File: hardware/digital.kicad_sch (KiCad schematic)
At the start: 0 parts

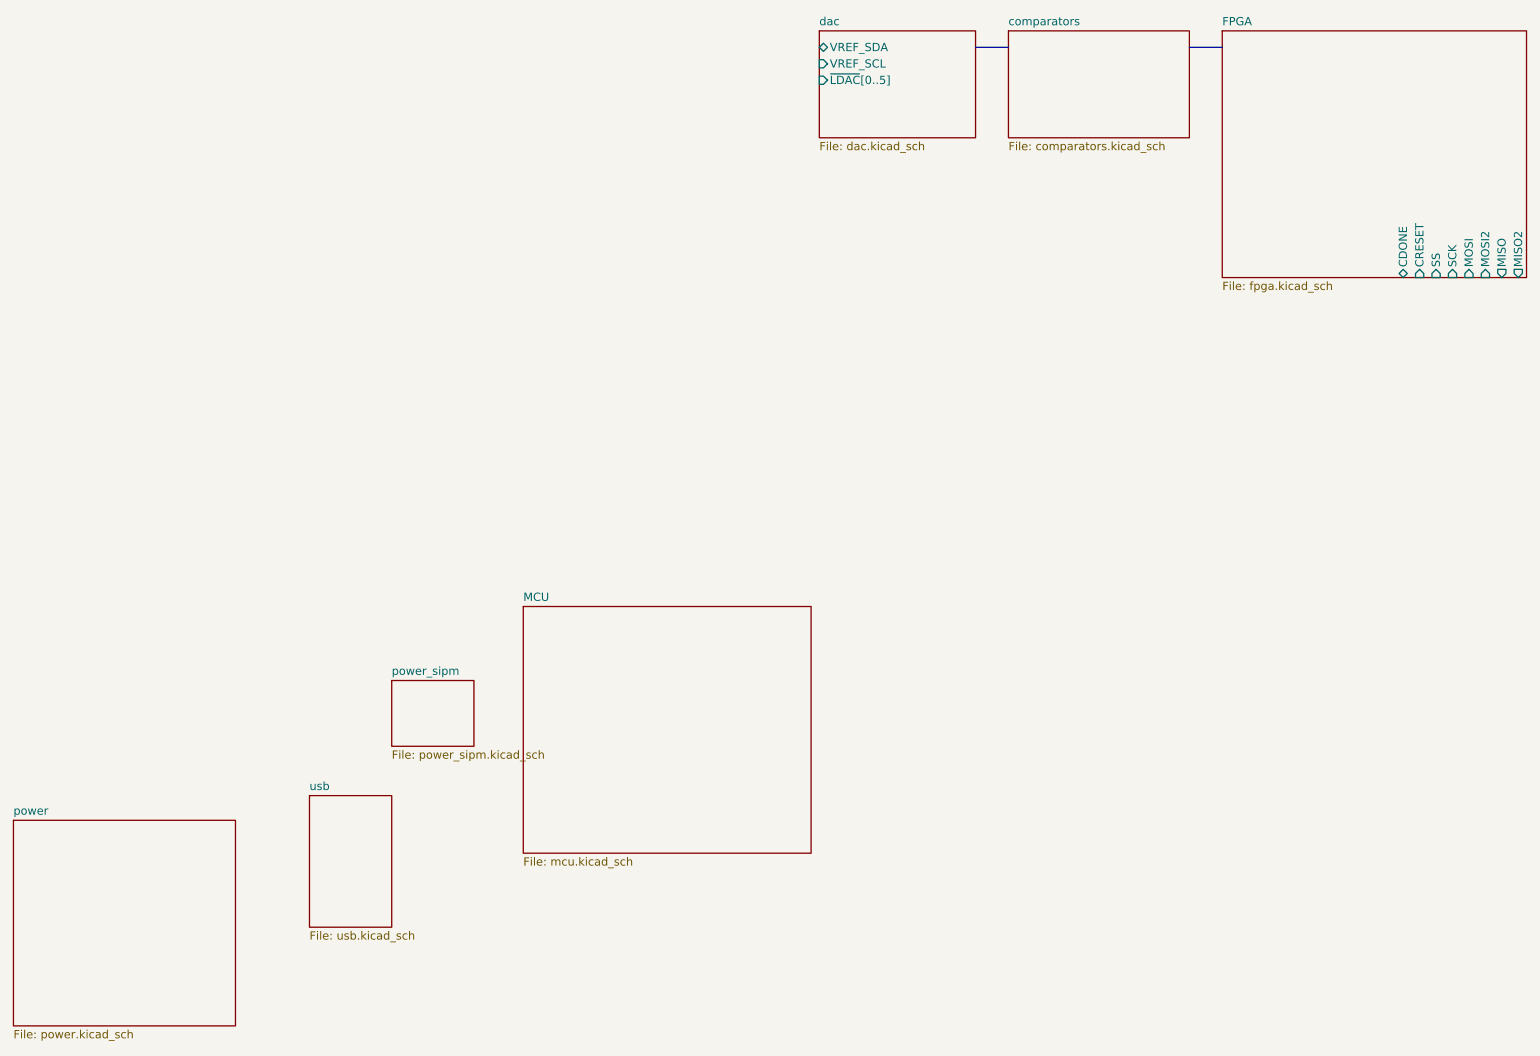
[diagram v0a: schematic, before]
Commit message: complete schematic wiring
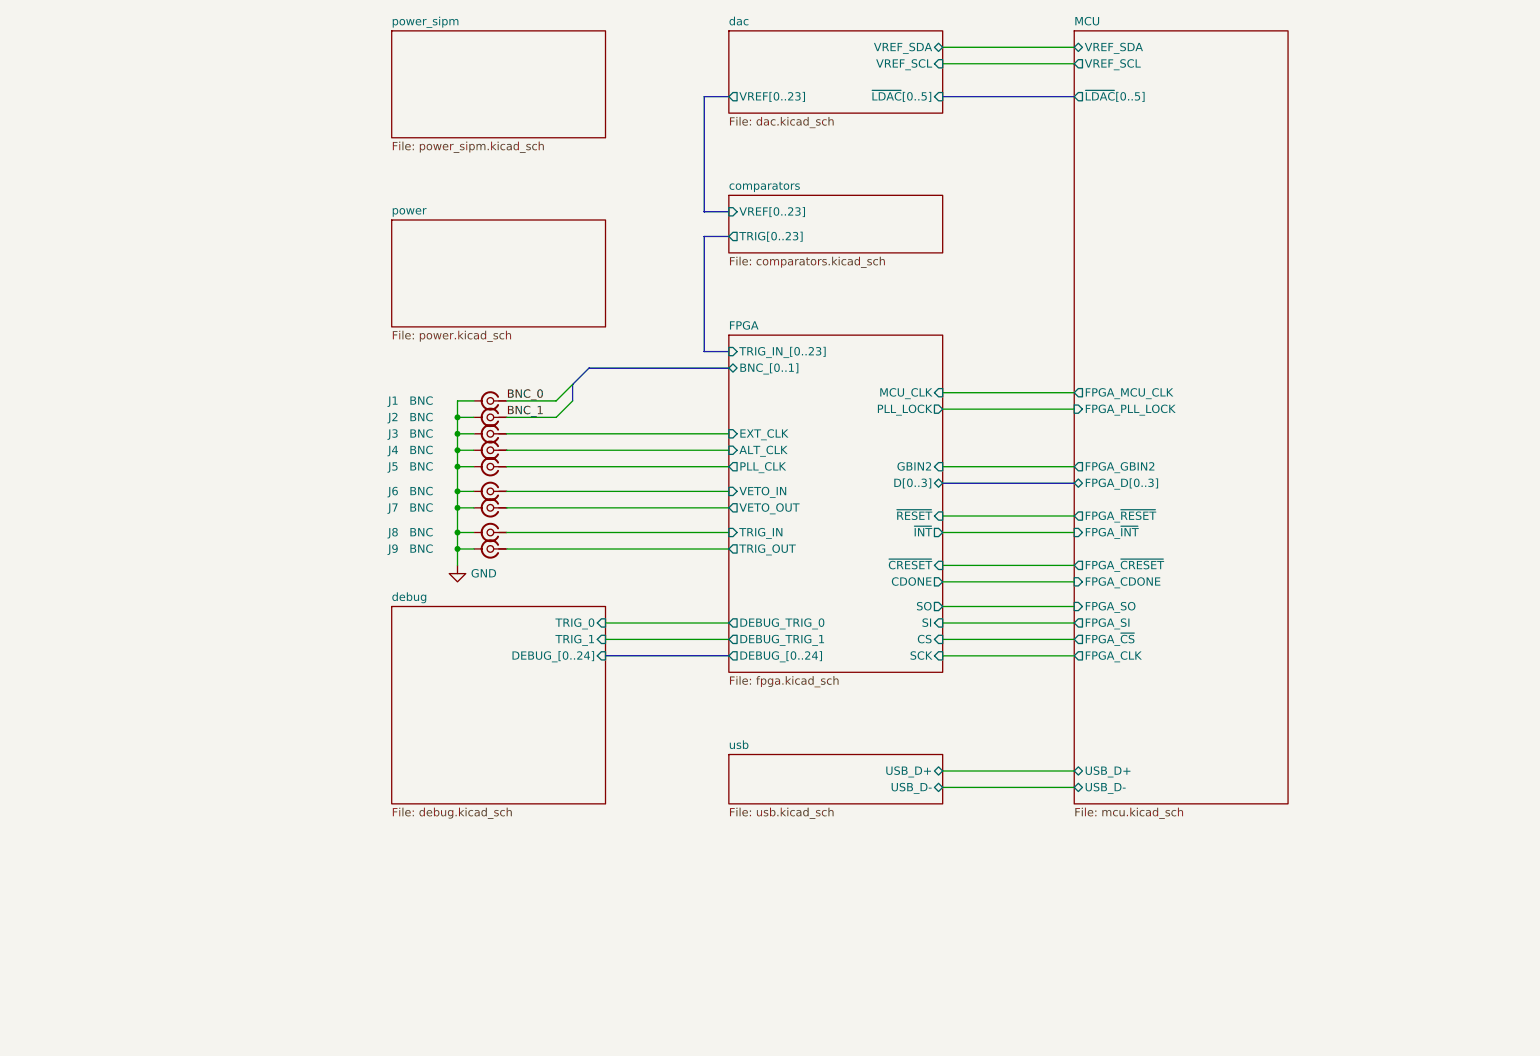
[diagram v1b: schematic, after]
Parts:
- added J1, J2, J3, J4, J5, J6, J7, J8, J9: BNC, symbol Connector:Conn_Coaxial_Small
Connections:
- new net BNC_0: J1.1 (In)
- new net BNC_1: J2.1 (In)
- new net FPGA/ALT_CLK: J4.1 (In)
- new net FPGA/EXT_CLK: J3.1 (In)
- new net FPGA/PLL_CLK: J5.1 (In)
- new net FPGA/TRIG_IN: J8.1 (In)
- new net FPGA/TRIG_OUT: J9.1 (In)
- new net FPGA/VETO_IN: J6.1 (In)
- new net FPGA/VETO_OUT: J7.1 (In)
- new net GND: J1.2 (Ext), J2.2 (Ext), J3.2 (Ext), J4.2 (Ext), J5.2 (Ext), J6.2 (Ext), J7.2 (Ext), J8.2 (Ext), J9.2 (Ext)
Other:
- added sheet debug (debug.kicad_sch)
- sheet FPGA ports: added ALT_CLK, BNC_[0..1], CS, DEBUG_TRIG_0, DEBUG_TRIG_1, DEBUG_[0..24], D[0..3], EXT_CLK, GBIN2, MCU_CLK, PLL_CLK, PLL_LOCK, SI, SO, TRIG_IN, TRIG_IN_[0..23], TRIG_OUT, VETO_IN, VETO_OUT, ~{CRESET}, ~{INT}, ~{RESET}; removed CRESET, MISO, MISO2, MOSI, MOSI2, SS
- sheet MCU ports: added FPGA_CDONE, FPGA_CLK, FPGA_D[0..3], FPGA_GBIN2, FPGA_MCU_CLK, FPGA_PLL_LOCK, FPGA_SI, FPGA_SO, FPGA_~{CRESET}, FPGA_~{CS}, FPGA_~{INT}, FPGA_~{RESET}, USB_D+, USB_D-, VREF_SCL, VREF_SDA, ~{LDAC}[0..5]; removed none
- sheet comparators ports: added TRIG[0..23], VREF[0..23]; removed none
- sheet dac ports: added VREF[0..23]; removed none
- sheet usb ports: added USB_D+, USB_D-; removed none

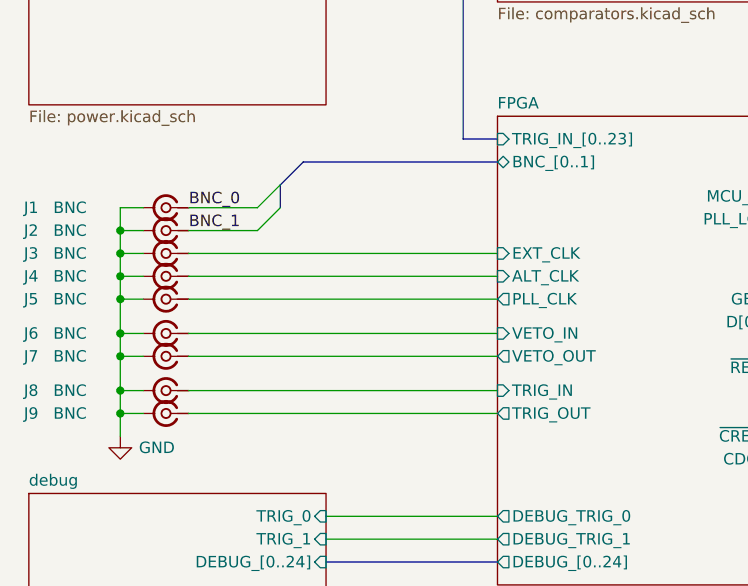
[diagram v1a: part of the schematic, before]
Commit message: update power system + add LCSC part numbers
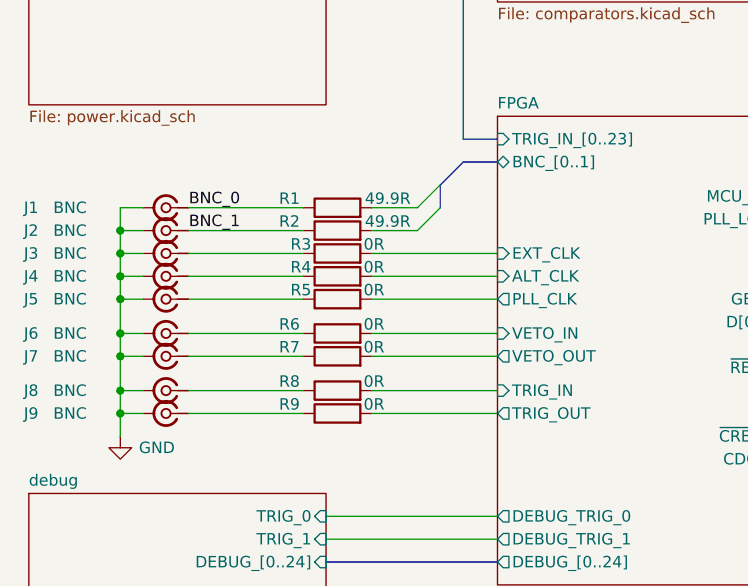
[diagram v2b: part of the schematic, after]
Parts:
- added R1, R2: 49.9R, Resistor_SMD:R_0402_1005Metric, symbol Device:R
- added R3, R4, R5, R6, R7, R8, R9: 0R, Resistor_SMD:R_0402_1005Metric, symbol Device:R
- J1, J2, J3, J4, J5, J6, J7, J8, J9: footprint (none) -> Connector_Coaxial:BNC_TEConnectivity_1478204_Vertical
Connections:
- net BNC_0: now also R1.1
- net BNC_1: now also R2.1
- net FPGA/ALT_CLK: now also R4.2; no longer J4.1 (In)
- net FPGA/EXT_CLK: now also R3.2; no longer J3.1 (In)
- net FPGA/PLL_CLK: now also R5.2; no longer J5.1 (In)
- net FPGA/TRIG_IN: now also R8.2; no longer J8.1 (In)
- net FPGA/TRIG_OUT: now also R9.2; no longer J9.1 (In)
- net FPGA/VETO_IN: now also R6.2; no longer J6.1 (In)
- net FPGA/VETO_OUT: now also R7.2; no longer J7.1 (In)
- new net: J5.1 (In), R5.1
- new net: J3.1 (In), R3.1
- new net: J7.1 (In), R7.1
- new net: J9.1 (In), R9.1
- new net: J4.1 (In), R4.1
- new net: J8.1 (In), R8.1
- new net: J6.1 (In), R6.1

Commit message: apply manufacturing BOM
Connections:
- net BNC_0: now also R1.2; no longer J1.1 (In), R1.1
- net BNC_1: now also R2.2; no longer J2.1 (In), R2.1
- new net: J1.1 (In), R1.1
- new net: J2.1 (In), R2.1
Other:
- moved on the sheet: R1, R2, R3, R4, R5, R6, R7, R8, R9

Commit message: route digital inputs
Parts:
- J1, J2, J3, J4, J5, J6, J7, J8, J9: footprint Connector_Coaxial:BNC_TEConnectivity_1478204_Vertical -> digital:BNC_TEConnectivity_1478204_Vertical
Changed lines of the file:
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@@
 			)
 		)
-		(property "Footprint" "Connector_Coaxial:BNC_TEConnectivity_1478204_Vertical"
+		(property "Footprint" "digital:BNC_TEConnectivity_1478204_Vertical"
 			(at 93.98 101.6 0)
 			(effects
@@
 			)
 		)
-		(property "Footprint" "Connector_Coaxial:BNC_TEConnectivity_1478204_Vertical"
+		(property "Footprint" "digital:BNC_TEConnectivity_1478204_Vertical"
 			(at 93.98 96.52 0)
 			(effects
@@
 			)
 		)
-		(property "Footprint" "Connector_Coaxial:BNC_TEConnectivity_1478204_Vertical"
+		(property "Footprint" "digital:BNC_TEConnectivity_1478204_Vertical"
 			(at 93.98 107.95 0)
 			(effects
@@
 			)
 		)
-		(property "Footprint" "Connector_Coaxial:BNC_TEConnectivity_1478204_Vertical"
+		(property "Footprint" "digital:BNC_TEConnectivity_1478204_Vertical"
 			(at 93.98 91.44 0)
 			(effects
@@
 			)
 		)
-		(property "Footprint" "Connector_Coaxial:BNC_TEConnectivity_1478204_Vertical"
+		(property "Footprint" "digital:BNC_TEConnectivity_1478204_Vertical"
 			(at 93.98 93.98 0)
 			(effects
@@
 			)
 		)
-		(property "Footprint" "Connector_Coaxial:BNC_TEConnectivity_1478204_Vertical"
+		(property "Footprint" "digital:BNC_TEConnectivity_1478204_Vertical"
 			(at 93.98 111.76 0)
 			(effects
@@
 			)
 		)
-		(property "Footprint" "Connector_Coaxial:BNC_TEConnectivity_1478204_Vertical"
+		(property "Footprint" "digital:BNC_TEConnectivity_1478204_Vertical"
 			(at 93.98 114.3 0)
 			(effects
@@
 			)
 		)
-		(property "Footprint" "Connector_Coaxial:BNC_TEConnectivity_1478204_Vertical"
+		(property "Footprint" "digital:BNC_TEConnectivity_1478204_Vertical"
 			(at 93.98 99.06 0)
 			(effects
@@
 			)
 		)
-		(property "Footprint" "Connector_Coaxial:BNC_TEConnectivity_1478204_Vertical"
+		(property "Footprint" "digital:BNC_TEConnectivity_1478204_Vertical"
 			(at 93.98 105.41 0)
 			(effects

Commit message: route more
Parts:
- J1, J3, J6, J7, J8, J9: footprint digital:BNC_TEConnectivity_1478204_Vertical -> digital:DOSIN-801-0078
- J2, J4, J5: value BNC -> IPEX-1; footprint digital:BNC_TEConnectivity_1478204_Vertical -> digital:BWIPX-1-001E; LCSC (none) -> C496552
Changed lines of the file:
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@@
 			)
 		)
-		(property "Value" "BNC"
+		(property "Value" "IPEX-1"
 			(at 83.312 101.6 0)
 			(effects
@@
 			)
 		)
-		(property "Footprint" "digital:BNC_TEConnectivity_1478204_Vertical"
+		(property "Footprint" "digital:BWIPX-1-001E"
 			(at 93.98 101.6 0)
 			(effects
@@
 		)
 		(property "Description" "small coaxial connector (BNC, SMA, SMB, SMC, Cinch/RCA, LEMO, ...)"
+			(at 93.98 101.6 0)
+			(effects
+				(font
+					(size 1.27 1.27)
+				)
+				(hide yes)
+			)
+		)
+		(property "LCSC" "C496552"
 			(at 93.98 101.6 0)
 			(effects
@@
 			)
 		)
-		(property "Footprint" "digital:BNC_TEConnectivity_1478204_Vertical"
+		(property "Footprint" "digital:DOSIN-801-0078"
 			(at 93.98 96.52 0)
 			(effects
@@
 			)
 		)
-		(property "Footprint" "digital:BNC_TEConnectivity_1478204_Vertical"
+		(property "Footprint" "digital:DOSIN-801-0078"
 			(at 93.98 107.95 0)
 			(effects
@@
 			)
 		)
-		(property "Footprint" "digital:BNC_TEConnectivity_1478204_Vertical"
+		(property "Footprint" "digital:DOSIN-801-0078"
 			(at 93.98 91.44 0)
 			(effects
@@
 			)
 		)
-		(property "Value" "BNC"
+		(property "Value" "IPEX-1"
 			(at 83.312 93.98 0)
 			(effects
@@
 			)
 		)
-		(property "Footprint" "digital:BNC_TEConnectivity_1478204_Vertical"
+		(property "Footprint" "digital:BWIPX-1-001E"
 			(at 93.98 93.98 0)
 			(effects
@@
 		)
 		(property "Description" "small coaxial connector (BNC, SMA, SMB, SMC, Cinch/RCA, LEMO, ...)"
+			(at 93.98 93.98 0)
+			(effects
+				(font
+					(size 1.27 1.27)
+				)
+				(hide yes)
+			)
+		)
+		(property "LCSC" "C496552"
 			(at 93.98 93.98 0)
 			(effects
@@
 			)
 		)
-		(property "Footprint" "digital:BNC_TEConnectivity_1478204_Vertical"
+		(property "Footprint" "digital:DOSIN-801-0078"
 			(at 93.98 111.76 0)
 			(effects
@@
 			)
 		)
-		(property "Footprint" "digital:BNC_TEConnectivity_1478204_Vertical"
+		(property "Footprint" "digital:DOSIN-801-0078"
 			(at 93.98 114.3 0)
 			(effects
@@
 			)
 		)
-		(property "Value" "BNC"
+		(property "Value" "IPEX-1"
 			(at 83.312 99.06 0)
 			(effects
@@
 			)
 		)
-		(property "Footprint" "digital:BNC_TEConnectivity_1478204_Vertical"
+		(property "Footprint" "digital:BWIPX-1-001E"
 			(at 93.98 99.06 0)
 			(effects
@@
 		)
 		(property "Description" "small coaxial connector (BNC, SMA, SMB, SMC, Cinch/RCA, LEMO, ...)"
+			(at 93.98 99.06 0)
+			(effects
+				(font
+					(size 1.27 1.27)
+				)
+				(hide yes)
+			)
+		)
+		(property "LCSC" "C496552"
 			(at 93.98 99.06 0)
 			(effects
@@
 			)
 		)
-		(property "Footprint" "digital:BNC_TEConnectivity_1478204_Vertical"
+		(property "Footprint" "digital:DOSIN-801-0078"
 			(at 93.98 105.41 0)
 			(effects

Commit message: route mcu
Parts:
- J1, J3, J6, J7, J8, J9: value BNC -> IPEX-1; footprint digital:DOSIN-801-0078 -> digital:BWIPX-1-001E; LCSC (none) -> C496552
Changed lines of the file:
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@@
 			)
 		)
-		(property "Value" "BNC"
+		(property "Value" "IPEX-1"
 			(at 83.312 96.52 0)
 			(effects
@@
 			)
 		)
-		(property "Footprint" "digital:DOSIN-801-0078"
+		(property "Footprint" "digital:BWIPX-1-001E"
 			(at 93.98 96.52 0)
 			(effects
@@
 		)
 		(property "Description" "small coaxial connector (BNC, SMA, SMB, SMC, Cinch/RCA, LEMO, ...)"
+			(at 93.98 96.52 0)
+			(effects
+				(font
+					(size 1.27 1.27)
+				)
+				(hide yes)
+			)
+		)
+		(property "LCSC" "C496552"
 			(at 93.98 96.52 0)
 			(effects
@@
 			)
 		)
-		(property "Value" "BNC"
+		(property "Value" "IPEX-1"
 			(at 83.312 107.95 0)
 			(effects
@@
 			)
 		)
-		(property "Footprint" "digital:DOSIN-801-0078"
+		(property "Footprint" "digital:BWIPX-1-001E"
 			(at 93.98 107.95 0)
 			(effects
@@
 		)
 		(property "Description" "small coaxial connector (BNC, SMA, SMB, SMC, Cinch/RCA, LEMO, ...)"
+			(at 93.98 107.95 0)
+			(effects
+				(font
+					(size 1.27 1.27)
+				)
+				(hide yes)
+			)
+		)
+		(property "LCSC" "C496552"
 			(at 93.98 107.95 0)
 			(effects
@@
 			)
 		)
-		(property "Value" "BNC"
+		(property "Value" "IPEX-1"
 			(at 83.312 91.44 0)
 			(effects
@@
 			)
 		)
-		(property "Footprint" "digital:DOSIN-801-0078"
+		(property "Footprint" "digital:BWIPX-1-001E"
 			(at 93.98 91.44 0)
 			(effects
@@
 		)
 		(property "Description" "small coaxial connector (BNC, SMA, SMB, SMC, Cinch/RCA, LEMO, ...)"
+			(at 93.98 91.44 0)
+			(effects
+				(font
+					(size 1.27 1.27)
+				)
+				(hide yes)
+			)
+		)
+		(property "LCSC" "C496552"
 			(at 93.98 91.44 0)
 			(effects
@@
 			)
 		)
-		(property "Value" "BNC"
+		(property "Value" "IPEX-1"
 			(at 83.312 111.76 0)
 			(effects
@@
 			)
 		)
-		(property "Footprint" "digital:DOSIN-801-0078"
+		(property "Footprint" "digital:BWIPX-1-001E"
 			(at 93.98 111.76 0)
 			(effects
@@
 		)
 		(property "Description" "small coaxial connector (BNC, SMA, SMB, SMC, Cinch/RCA, LEMO, ...)"
+			(at 93.98 111.76 0)
+			(effects
+				(font
+					(size 1.27 1.27)
+				)
+				(hide yes)
+			)
+		)
+		(property "LCSC" "C496552"
 			(at 93.98 111.76 0)
 			(effects
@@
 			)
 		)
-		(property "Value" "BNC"
+		(property "Value" "IPEX-1"
 			(at 83.312 114.3 0)
 			(effects
@@
 			)
 		)
-		(property "Footprint" "digital:DOSIN-801-0078"
+		(property "Footprint" "digital:BWIPX-1-001E"
 			(at 93.98 114.3 0)
 			(effects
@@
 		)
 		(property "Description" "small coaxial connector (BNC, SMA, SMB, SMC, Cinch/RCA, LEMO, ...)"
+			(at 93.98 114.3 0)
+			(effects
+				(font
+					(size 1.27 1.27)
+				)
+				(hide yes)
+			)
+		)
+		(property "LCSC" "C496552"
 			(at 93.98 114.3 0)
 			(effects
@@
 			)
 		)
-		(property "Value" "BNC"
+		(property "Value" "IPEX-1"
 			(at 83.312 105.41 0)
 			(effects
@@
 			)
 		)
-		(property "Footprint" "digital:DOSIN-801-0078"
+		(property "Footprint" "digital:BWIPX-1-001E"
 			(at 93.98 105.41 0)
 			(effects
@@
 			(at 93.98 105.41 0)
 			(effects
+				(font
+					(size 1.27 1.27)
+				)
+				(hide yes)
+			)
+		)
+		(property "LCSC" "C496552"
+			(at 93.98 105.41 0)
+			(effects

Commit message: route
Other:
- removed sheet power_sipm
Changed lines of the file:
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@@
-	)
-	(sheet
-		(at 78.74 34.29)
-		(size 33.02 16.51)
-		(exclude_from_sim no)
-		(in_bom yes)
-		(on_board yes)
-		(dnp no)
-		(fields_autoplaced yes)
-		(stroke
-			(width 0.1524)
-			(type solid)
-		)
-		(fill
-			(color 0 0 0 0.0000)
-		)
-		(property "Sheetname" "power_sipm"
-			(at 78.74 33.5784 0)
-			(effects
-				(font
-					(size 1.27 1.27)
-				)
-				(justify left bottom)
-			)
-		)
-		(property "Sheetfile" "power_sipm.kicad_sch"
-			(at 78.74 51.3846 0)
-			(effects
-				(font
-					(size 1.27 1.27)
-				)
-				(justify left top)
-			)
-		)
-		(instances
-			(project "digital"
-				(path "/4c5c7ce5-09d6-4a32-b2a0-f32b0c47f27d"
-					(page "8")
-				)
-			)
-		)
 	)
 	(sheet
@@
 	)
 	(sheet
-		(at 78.74 63.5)
-		(size 33.02 16.51)
+		(at 78.74 34.29)
+		(size 33.02 45.72)
 		(exclude_from_sim no)
 		(in_bom yes)
@@
 		)
 		(property "Sheetname" "power"
-			(at 78.74 62.7884 0)
-			(effects
-				(font
+			(at 78.74 33.5784 0)
+			(effects
+				(font
